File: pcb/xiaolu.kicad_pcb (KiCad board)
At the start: 2 copper layers, 51 x 76 mm, 41 parts, among them J1 Conn_01x04_Male, J2 TRRS, SW1 SW_Push, SW10 SW_Push, SW11 SW_Push, SW12 SW_Push, SW13 SW_Push, SW14 SW_Push, SW15 SW_Push, SW16 SW_Push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

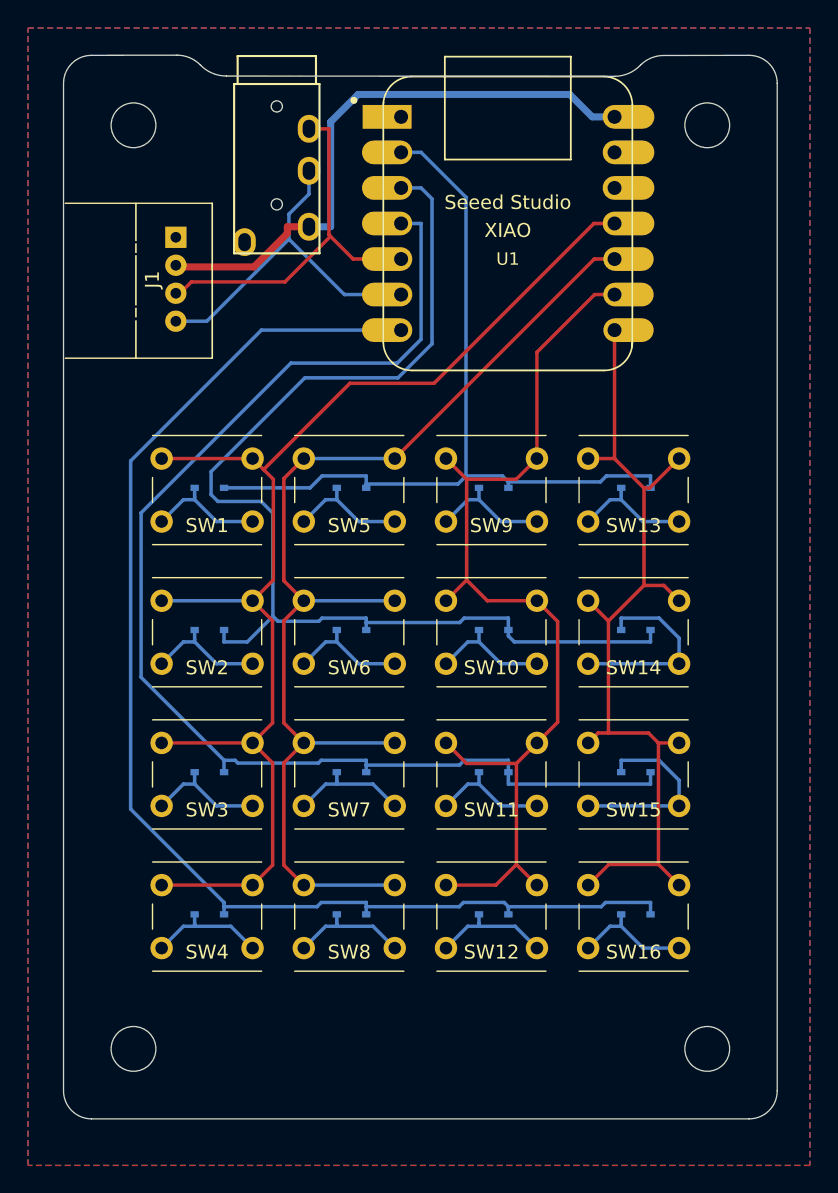
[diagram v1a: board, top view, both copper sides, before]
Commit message: add optional pull-up registers to I2C SDA/SCL
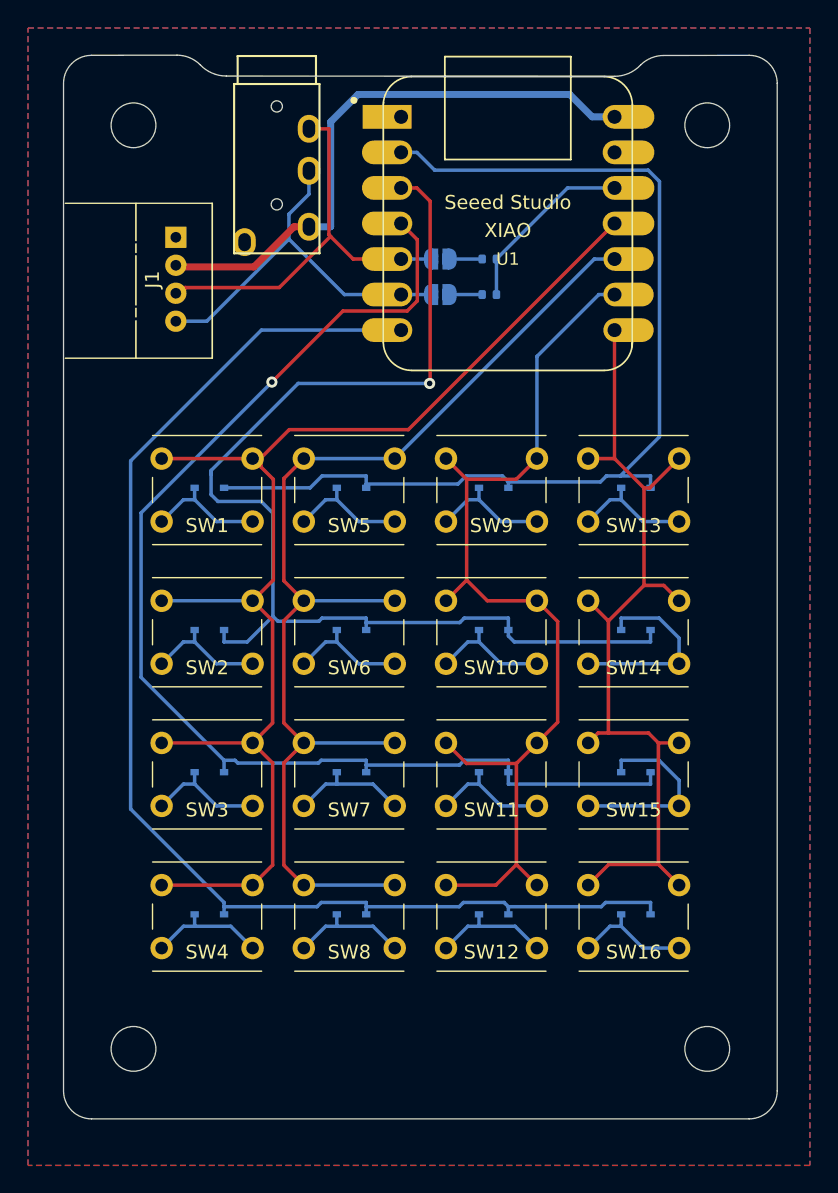
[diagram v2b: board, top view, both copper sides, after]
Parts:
- added JP1: SolderJumper_2_Open, Jumper:SolderJumper-2_P1.3mm_Open_RoundedPad1.0x1.5mm, B.Cu at (77.7, 64.8)
- added JP2: SolderJumper_2_Open, Jumper:SolderJumper-2_P1.3mm_Open_RoundedPad1.0x1.5mm, B.Cu at (77.7, 67.3)
- added R1: 4.7k, Resistor_SMD:R_0402_1005Metric, B.Cu at (81.2, 64.8)
- added R2: 4.7k, Resistor_SMD:R_0402_1005Metric, B.Cu at (81.2, 67.3)
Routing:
- net row0: track 59.4 -> 75.1 mm
- net +3.3V: track 0.00 -> 13.1 mm
- net SDA: track 27.3 -> 30.3 mm
- net row2: track 90.0 -> 87.2 mm, vias 0 -> 1
- net SCL: track 25.3 -> 27.8 mm
- net Net-(R2-Pad1): track 0.00 -> 2.34 mm
- net Net-(JP1-Pad1): track 0.00 -> 2.34 mm
- net row1: track 82.0 -> 83.6 mm, vias 0 -> 1
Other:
- board text added: "${372774f6-de89-4169-86ba-469560644ca9:VALUE}"

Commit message: modify fill ground, its vias
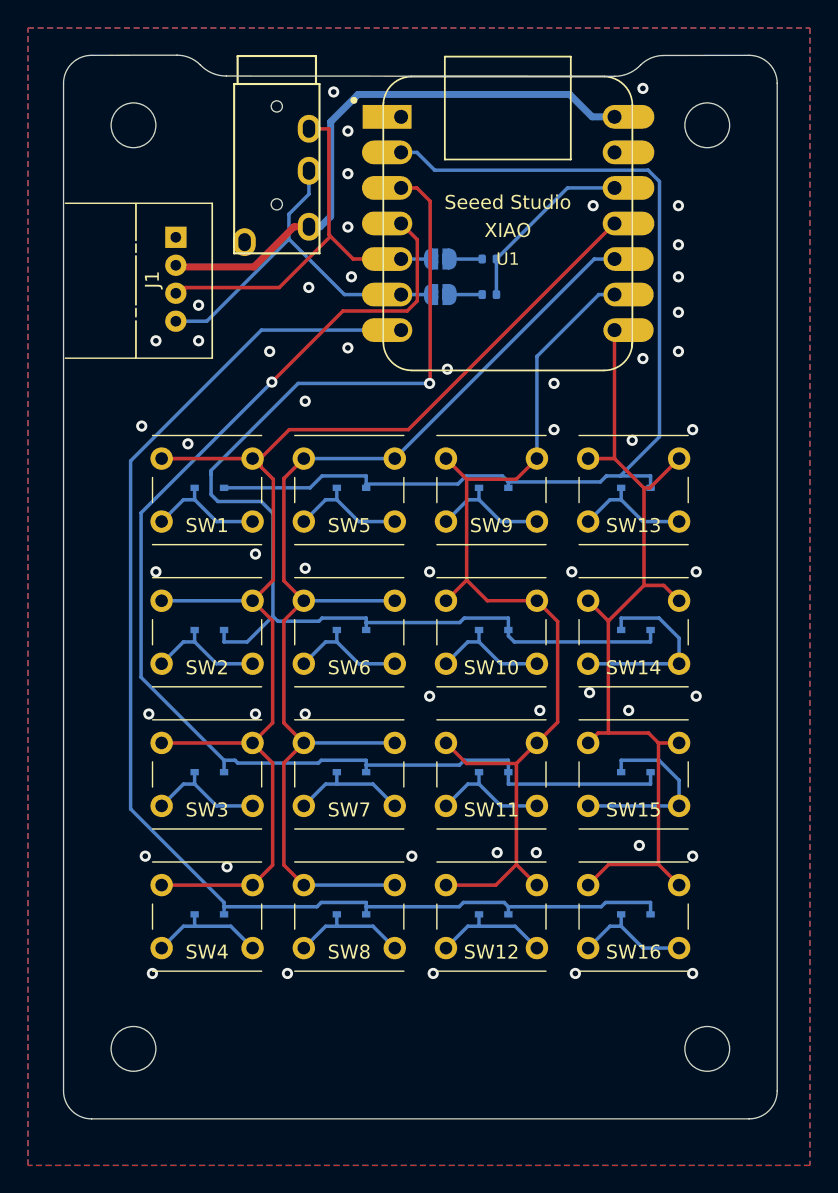
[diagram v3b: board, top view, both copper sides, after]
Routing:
- net GND: vias 0 -> 53
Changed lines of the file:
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@@
   (segment (start 89.8499 112.45) (end 88.29 114.01) (width 0.25) (layer "B.Cu") (net 20))
   (segment (start 94.79 114.01) (end 92.2099 114.01) (width 0.25) (layer "B.Cu") (net 20))
+  (via (at 91.186 97.028) (size 0.8) (drill 0.4) (layers "F.Cu" "B.Cu") (free) (net 21))
+  (via (at 96.012 87.122) (size 0.8) (drill 0.4) (layers "F.Cu" "B.Cu") (free) (net 21))
+  (via (at 66.802 115.824) (size 0.8) (drill 0.4) (layers "F.Cu" "B.Cu") (free) (net 21))
+  (via (at 59.69 77.978) (size 0.8) (drill 0.4) (layers "F.Cu" "B.Cu") (free) (net 21))
+  (via (at 76.962 96.012) (size 0.8) (drill 0.4) (layers "F.Cu" "B.Cu") (free) (net 21))
+  (via (at 81.788 107.188) (size 0.8) (drill 0.4) (layers "F.Cu" "B.Cu") (free) (net 21))
+  (via (at 56.642 107.442) (size 0.8) (drill 0.4) (layers "F.Cu" "B.Cu") (free) (net 21))
+  (via (at 92.202 71.882) (size 0.8) (drill 0.4) (layers "F.Cu" "B.Cu") (free) (net 21))
+  (via (at 57.404 70.612) (size 0.8) (drill 0.4) (layers "F.Cu" "B.Cu") (free) (net 21))
+  (via (at 92.202 52.578) (size 0.8) (drill 0.4) (layers "F.Cu" "B.Cu") (free) (net 21))
+  (via (at 91.44 77.724) (size 0.8) (drill 0.4) (layers "F.Cu" "B.Cu") (free) (net 21))
+  (via (at 68.072 74.93) (size 0.8) (drill 0.4) (layers "F.Cu" "B.Cu") (free) (net 21))
+  (via (at 91.948 106.68) (size 0.8) (drill 0.4) (layers "F.Cu" "B.Cu") (free) (net 21))
+  (via (at 76.962 87.122) (size 0.8) (drill 0.4) (layers "F.Cu" "B.Cu") (free) (net 21))
+  (via (at 68.072 86.868) (size 0.8) (drill 0.4) (layers "F.Cu" "B.Cu") (free) (net 21))
+  (via (at 96.012 96.012) (size 0.8) (drill 0.4) (layers "F.Cu" "B.Cu") (free) (net 21))
+  (via (at 68.326 66.802) (size 0.8) (drill 0.4) (layers "F.Cu" "B.Cu") (free) (net 21))
+  (via (at 65.532 71.374) (size 0.8) (drill 0.4) (layers "F.Cu" "B.Cu") (free) (net 21))
+  (via (at 88.646 60.96) (size 0.8) (drill 0.4) (layers "F.Cu" "B.Cu") (free) (net 21))
+  (via (at 84.836 97.028) (size 0.8) (drill 0.4) (layers "F.Cu" "B.Cu") (free) (net 21))
+  (via (at 87.376 115.824) (size 0.8) (drill 0.4) (layers "F.Cu" "B.Cu") (free) (net 21))
+  (via (at 56.896 97.282) (size 0.8) (drill 0.4) (layers "F.Cu" "B.Cu") (free) (net 21))
+  (via (at 62.484 108.204) (size 0.8) (drill 0.4) (layers "F.Cu" "B.Cu") (free) (net 21))
+  (via (at 85.852 76.962) (size 0.8) (drill 0.4) (layers "F.Cu" "B.Cu") (free) (net 21))
+  (via (at 71.12 55.626) (size 0.8) (drill 0.4) (layers "F.Cu" "B.Cu") (free) (net 21))
+  (via (at 75.692 107.442) (size 0.8) (drill 0.4) (layers "F.Cu" "B.Cu") (free) (net 21))
+  (via (at 70.104 52.832) (size 0.8) (drill 0.4) (layers "F.Cu" "B.Cu") (free) (net 21))
+  (via (at 71.374 66.04) (size 0.8) (drill 0.4) (layers "F.Cu" "B.Cu") (free) (net 21))
+  (via (at 95.758 107.442) (size 0.8) (drill 0.4) (layers "F.Cu" "B.Cu") (free) (net 21))
+  (via (at 94.742 66.04) (size 0.8) (drill 0.4) (layers "F.Cu" "B.Cu") (free) (net 21))
+  (via (at 95.758 76.962) (size 0.8) (drill 0.4) (layers "F.Cu" "B.Cu") (free) (net 21))
+  (via (at 87.122 87.122) (size 0.8) (drill 0.4) (layers "F.Cu" "B.Cu") (free) (net 21))
+  (via (at 94.742 68.58) (size 0.8) (drill 0.4) (layers "F.Cu" "B.Cu") (free) (net 21))
+  (via (at 60.452 68.072) (size 0.8) (drill 0.4) (layers "F.Cu" "B.Cu") (free) (net 21))
+  (via (at 57.404 87.122) (size 0.8) (drill 0.4) (layers "F.Cu" "B.Cu") (free) (net 21))
+  (via (at 57.15 115.824) (size 0.8) (drill 0.4) (layers "F.Cu" "B.Cu") (free) (net 21))
+  (via (at 71.12 58.674) (size 0.8) (drill 0.4) (layers "F.Cu" "B.Cu") (free) (net 21))
+  (via (at 64.516 85.852) (size 0.8) (drill 0.4) (layers "F.Cu" "B.Cu") (free) (net 21))
+  (via (at 64.516 97.282) (size 0.8) (drill 0.4) (layers "F.Cu" "B.Cu") (free) (net 21))
+  (via (at 95.758 115.824) (size 0.8) (drill 0.4) (layers "F.Cu" "B.Cu") (free) (net 21))
+  (via (at 71.12 62.484) (size 0.8) (drill 0.4) (layers "F.Cu" "B.Cu") (free) (net 21))
+  (via (at 85.852 73.66) (size 0.8) (drill 0.4) (layers "F.Cu" "B.Cu") (free) (net 21))
+  (via (at 88.392 95.758) (size 0.8) (drill 0.4) (layers "F.Cu" "B.Cu") (free) (net 21))
+  (via (at 94.742 63.754) (size 0.8) (drill 0.4) (layers "F.Cu" "B.Cu") (free) (net 21))
+  (via (at 60.452 70.612) (size 0.8) (drill 0.4) (layers "F.Cu" "B.Cu") (free) (net 21))
+  (via (at 94.742 71.374) (size 0.8) (drill 0.4) (layers "F.Cu" "B.Cu") (free) (net 21))
+  (via (at 68.072 97.282) (size 0.8) (drill 0.4) (layers "F.Cu" "B.Cu") (free) (net 21))
+  (via (at 94.742 60.96) (size 0.8) (drill 0.4) (layers "F.Cu" "B.Cu") (free) (net 21))
+  (via (at 78.232 72.644) (size 0.8) (drill 0.4) (layers "F.Cu" "B.Cu") (free) (net 21))
+  (via (at 56.388 76.708) (size 0.8) (drill 0.4) (layers "F.Cu" "B.Cu") (free) (net 21))
+  (via (at 77.216 115.824) (size 0.8) (drill 0.4) (layers "F.Cu" "B.Cu") (free) (net 21))
+  (via (at 84.582 107.188) (size 0.8) (drill 0.4) (layers "F.Cu" "B.Cu") (free) (net 21))
+  (via (at 71.12 71.12) (size 0.8) (drill 0.4) (layers "F.Cu" "B.Cu") (free) (net 21))
   (segment (start 59.2514 65.3364) (end 59.1907 65.2757) (width 0.5) (layer "F.Cu") (net 22))
   (segment (start 58.8857 65.2757) (end 58.825 65.215) (width 0.25) (layer "F.Cu") (net 22))
@@
   (segment (start 71.8467 53.0098) (end 69.8901 54.9664) (width 0.5) (layer "B.Cu") (net 22))
   (segment (start 86.9747 53.0098) (end 71.8467 53.0098) (width 0.5) (layer "B.Cu") (net 22))
+  (segment (start 69.8901 61.722) (end 69.1479 62.4642) (width 0.5) (layer "B.Cu") (net 22))
   (segment (start 90.175 54.61) (end 88.5749 54.61) (width 0.5) (layer "B.Cu") (net 22))
+  (segment (start 69.8901 54.9664) (end 69.8901 61.722) (width 0.5) (layer "B.Cu") (net 22))
+  (segment (start 69.1479 62.4642) (end 68.34 62.4642) (width 0.5) (layer "B.Cu") (net 22))
   (segment (start 88.5749 54.61) (end 86.9747 53.0098) (width 0.5) (layer "B.Cu") (net 22))
-  (segment (start 69.8901 54.9664) (end 69.8901 62.4642) (width 0.5) (layer "B.Cu") (net 22))
-  (segment (start 69.8901 62.4642) (end 68.34 62.4642) (width 0.5) (layer "B.Cu") (net 22))
   (segment (start 69.7651 63.0352) (end 69.8783 63.1483) (width 0.25) (layer "F.Cu") (net 23))
   (segment (start 66.2171 66.8095) (end 59.5355 66.8095) (width 0.25) (layer "F.Cu") (net 23))
@@
   (zone (net 21) (net_name "GND") (layers F&B.Cu) (hatch edge 0.508)
     (connect_pads (clearance 0.508))
-    (min_thickness 0.254) (filled_areas_thickness no)
-    (fill yes (thermal_gap 0.508) (thermal_bridge_width 0.508))
+    (min_thickness 0.508) (filled_areas_thickness no)
+    (fill yes (thermal_gap 0.508) (thermal_bridge_width 1.016))
     (polygon
       (pts
@@
       )
     )
+  )
+  (zone (net 0) (net_name "") (layer "B.Cu") (hatch edge 0.508)
+    (connect_pads (clearance 0))
+    (min_thickness 0.508)
+    (keepout (tracks allowed) (vias allowed) (pads allowed) (copperpour not_allowed) (footprints allowed))
+    (fill (thermal_gap 0.508) (thermal_bridge_width 1.016))
+    (polygon
+      (pts
+        (xy 91.186 59.69)
+        (xy 72.644 59.69)
+        (xy 72.644 47.244)
+        (xy 91.186 47.244)
+      )
+    )

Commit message: fix silk and GND vias
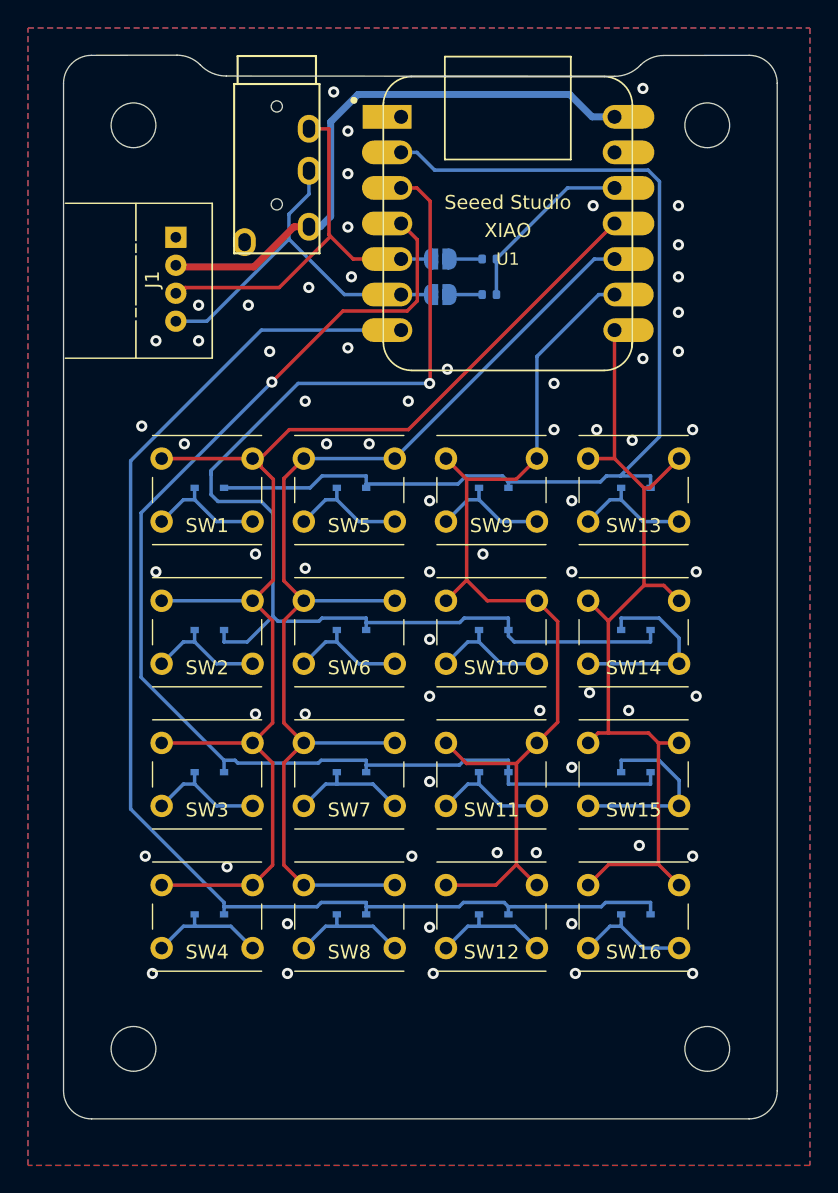
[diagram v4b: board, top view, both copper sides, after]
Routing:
- net GND: vias 53 -> 66
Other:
- board text added: "Port.A GND 5V SDA(5) SCL(6)"
- board text removed: "GND 5V SDA/GP5 SCL/GP6"
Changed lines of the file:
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@@
     (effects (font (size 0.8 0.8) (thickness 0.15)) (justify right mirror))
   )
-  (gr_text "GND\n5V\nSDA/GP5\nSCL/GP6" (at 57.15 66.04) (layer "B.SilkS")
-    (effects (font (size 0.8 0.8) (thickness 0.15)) (justify left mirror))
+  (gr_text "Port.A\nGND\n5V\nSDA(5)\nSCL(6)" (at 57.15 66.04) (layer "B.SilkS")
+    (effects (font (size 1 1) (thickness 0.15)) (justify left mirror))
   )
   (gr_text "R2:SDA\nR1:SCL\nT:5V\nS:GND" (at 65.405 57.3767) (layer "B.SilkS")
@@
   (via (at 96.012 87.122) (size 0.8) (drill 0.4) (layers "F.Cu" "B.Cu") (free) (net 21))
   (via (at 66.802 115.824) (size 0.8) (drill 0.4) (layers "F.Cu" "B.Cu") (free) (net 21))
-  (via (at 59.69 77.978) (size 0.8) (drill 0.4) (layers "F.Cu" "B.Cu") (free) (net 21))
+  (via (at 59.436 77.978) (size 0.8) (drill 0.4) (layers "F.Cu" "B.Cu") (free) (net 21))
+  (via (at 88.9 76.962) (size 0.8) (drill 0.4) (layers "F.Cu" "B.Cu") (free) (net 21))
   (via (at 76.962 96.012) (size 0.8) (drill 0.4) (layers "F.Cu" "B.Cu") (free) (net 21))
   (via (at 81.788 107.188) (size 0.8) (drill 0.4) (layers "F.Cu" "B.Cu") (free) (net 21))
+  (via (at 64.008 68.072) (size 0.8) (drill 0.4) (layers "F.Cu" "B.Cu") (free) (net 21))
   (via (at 56.642 107.442) (size 0.8) (drill 0.4) (layers "F.Cu" "B.Cu") (free) (net 21))
   (via (at 92.202 71.882) (size 0.8) (drill 0.4) (layers "F.Cu" "B.Cu") (free) (net 21))
   (via (at 57.404 70.612) (size 0.8) (drill 0.4) (layers "F.Cu" "B.Cu") (free) (net 21))
+  (via (at 76.962 102.108) (size 0.8) (drill 0.4) (layers "F.Cu" "B.Cu") (free) (net 21))
+  (via (at 80.772 85.852) (size 0.8) (drill 0.4) (layers "F.Cu" "B.Cu") (free) (net 21))
+  (via (at 76.962 82.042) (size 0.8) (drill 0.4) (layers "F.Cu" "B.Cu") (free) (net 21))
   (via (at 92.202 52.578) (size 0.8) (drill 0.4) (layers "F.Cu" "B.Cu") (free) (net 21))
   (via (at 91.44 77.724) (size 0.8) (drill 0.4) (layers "F.Cu" "B.Cu") (free) (net 21))
@@
   (via (at 68.072 86.868) (size 0.8) (drill 0.4) (layers "F.Cu" "B.Cu") (free) (net 21))
   (via (at 96.012 96.012) (size 0.8) (drill 0.4) (layers "F.Cu" "B.Cu") (free) (net 21))
+  (via (at 87.122 82.042) (size 0.8) (drill 0.4) (layers "F.Cu" "B.Cu") (free) (net 21))
   (via (at 68.326 66.802) (size 0.8) (drill 0.4) (layers "F.Cu" "B.Cu") (free) (net 21))
   (via (at 65.532 71.374) (size 0.8) (drill 0.4) (layers "F.Cu" "B.Cu") (free) (net 21))
   (via (at 88.646 60.96) (size 0.8) (drill 0.4) (layers "F.Cu" "B.Cu") (free) (net 21))
   (via (at 84.836 97.028) (size 0.8) (drill 0.4) (layers "F.Cu" "B.Cu") (free) (net 21))
+  (via (at 75.438 74.93) (size 0.8) (drill 0.4) (layers "F.Cu" "B.Cu") (free) (net 21))
   (via (at 87.376 115.824) (size 0.8) (drill 0.4) (layers "F.Cu" "B.Cu") (free) (net 21))
-  (via (at 56.896 97.282) (size 0.8) (drill 0.4) (layers "F.Cu" "B.Cu") (free) (net 21))
   (via (at 62.484 108.204) (size 0.8) (drill 0.4) (layers "F.Cu" "B.Cu") (free) (net 21))
   (via (at 85.852 76.962) (size 0.8) (drill 0.4) (layers "F.Cu" "B.Cu") (free) (net 21))
@@
   (via (at 95.758 107.442) (size 0.8) (drill 0.4) (layers "F.Cu" "B.Cu") (free) (net 21))
   (via (at 94.742 66.04) (size 0.8) (drill 0.4) (layers "F.Cu" "B.Cu") (free) (net 21))
+  (via (at 69.596 77.978) (size 0.8) (drill 0.4) (layers "F.Cu" "B.Cu") (free) (net 21))
+  (via (at 72.644 77.978) (size 0.8) (drill 0.4) (layers "F.Cu" "B.Cu") (free) (net 21))
   (via (at 95.758 76.962) (size 0.8) (drill 0.4) (layers "F.Cu" "B.Cu") (free) (net 21))
   (via (at 87.122 87.122) (size 0.8) (drill 0.4) (layers "F.Cu" "B.Cu") (free) (net 21))
@@
   (via (at 57.404 87.122) (size 0.8) (drill 0.4) (layers "F.Cu" "B.Cu") (free) (net 21))
   (via (at 57.15 115.824) (size 0.8) (drill 0.4) (layers "F.Cu" "B.Cu") (free) (net 21))
+  (via (at 66.802 112.268) (size 0.8) (drill 0.4) (layers "F.Cu" "B.Cu") (free) (net 21))
+  (via (at 87.122 112.268) (size 0.8) (drill 0.4) (layers "F.Cu" "B.Cu") (free) (net 21))
   (via (at 71.12 58.674) (size 0.8) (drill 0.4) (layers "F.Cu" "B.Cu") (free) (net 21))
   (via (at 64.516 85.852) (size 0.8) (drill 0.4) (layers "F.Cu" "B.Cu") (free) (net 21))
@@
   (via (at 94.742 63.754) (size 0.8) (drill 0.4) (layers "F.Cu" "B.Cu") (free) (net 21))
   (via (at 60.452 70.612) (size 0.8) (drill 0.4) (layers "F.Cu" "B.Cu") (free) (net 21))
+  (via (at 87.122 101.092) (size 0.8) (drill 0.4) (layers "F.Cu" "B.Cu") (free) (net 21))
   (via (at 94.742 71.374) (size 0.8) (drill 0.4) (layers "F.Cu" "B.Cu") (free) (net 21))
   (via (at 68.072 97.282) (size 0.8) (drill 0.4) (layers "F.Cu" "B.Cu") (free) (net 21))
@@
   (via (at 77.216 115.824) (size 0.8) (drill 0.4) (layers "F.Cu" "B.Cu") (free) (net 21))
   (via (at 84.582 107.188) (size 0.8) (drill 0.4) (layers "F.Cu" "B.Cu") (free) (net 21))
+  (via (at 76.962 112.522) (size 0.8) (drill 0.4) (layers "F.Cu" "B.Cu") (free) (net 21))
+  (via (at 76.962 91.948) (size 0.8) (drill 0.4) (layers "F.Cu" "B.Cu") (free) (net 21))
   (via (at 71.12 71.12) (size 0.8) (drill 0.4) (layers "F.Cu" "B.Cu") (free) (net 21))
   (segment (start 59.2514 65.3364) (end 59.1907 65.2757) (width 0.5) (layer "F.Cu") (net 22))
